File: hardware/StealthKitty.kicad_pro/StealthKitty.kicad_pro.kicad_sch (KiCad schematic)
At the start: 0 parts

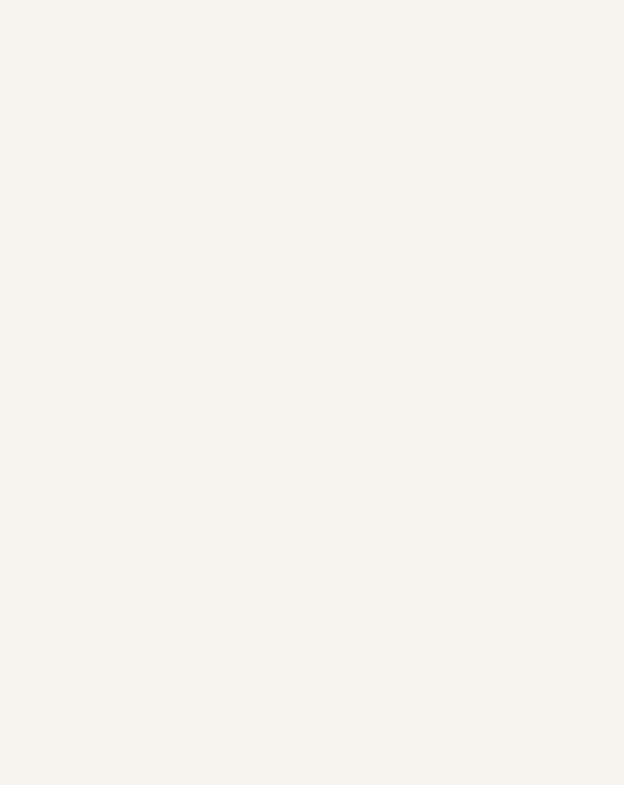
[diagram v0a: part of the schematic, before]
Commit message: réassignation pins stm32, ajout des modifs de la partie power, ajout des modfis de la revue de projet 02/10/24, modifs du 3/10/24 voir readme
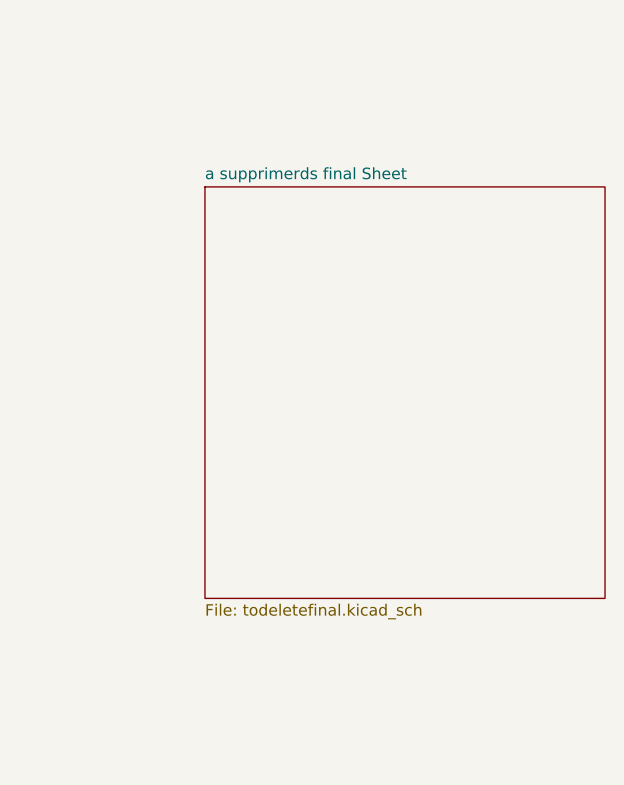
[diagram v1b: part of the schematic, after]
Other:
- added sheet a supprimerds final Sheet (todeletefinal.kicad_sch)
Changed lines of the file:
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@@
 	(paper "A4")
+	(sheet
+		(at 233.68 60.96)
+		(size 44.45 45.72)
+		(fields_autoplaced yes)
+		(stroke
+			(width 0.1524)
+			(type solid)
+		)
+		(fill
+			(color 0 0 0 0.0000)
+		)
+		(property "Sheetname" "a supprimerds final Sheet"
+			(at 233.68 60.2484 0)
+			(effects
+				(font
+					(size 1.27 1.27)
+				)
+				(justify left bottom)
+			)
+		)
+		(property "Sheetfile" "todeletefinal.kicad_sch"
+			(at 233.68 107.2646 0)
+			(effects
+				(font
+					(size 1.27 1.27)
+				)
+				(justify left top)
+			)
+		)
+		(instances
+			(project "StealthKitty.kicad_pro"
+				(path "/23d5732b-7ccb-40aa-85a2-3b18421ac23b"
+					(page "6")
+				)
+			)
+		)
+	)
 	(sheet
 		(at 55.88 31.75)
@@
 		)
 		(instances
-			(project "StealthKitty"
+			(project "StealthKitty.kicad_pro"
 				(path "/23d5732b-7ccb-40aa-85a2-3b18421ac23b"
 					(page "3")
@@
 		)
 		(instances
-			(project "StealthKitty"
+			(project "StealthKitty.kicad_pro"
 				(path "/23d5732b-7ccb-40aa-85a2-3b18421ac23b"
 					(page "4")
@@
 		)
 		(instances
-			(project "StealthKitty"
+			(project "StealthKitty.kicad_pro"
 				(path "/23d5732b-7ccb-40aa-85a2-3b18421ac23b"
 					(page "5")
@@
 		)
 		(instances
-			(project "StealthKitty"
+			(project "StealthKitty.kicad_pro"
 				(path "/23d5732b-7ccb-40aa-85a2-3b18421ac23b"
 					(page "3")

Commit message: suppression sous feuille 6,suppression dossier stealthkitty présent dans /hardware
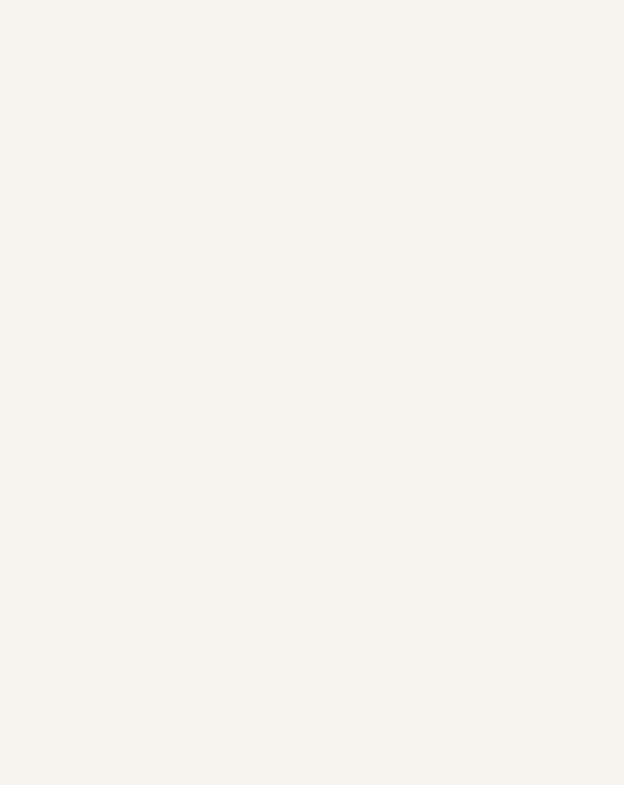
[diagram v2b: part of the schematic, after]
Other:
- removed sheet a supprimerds final Sheet
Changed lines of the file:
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@@
 	(paper "A4")
-	(sheet
-		(at 233.68 60.96)
-		(size 44.45 45.72)
-		(fields_autoplaced yes)
-		(stroke
-			(width 0.1524)
-			(type solid)
-		)
-		(fill
-			(color 0 0 0 0.0000)
-		)
-		(property "Sheetname" "a supprimerds final Sheet"
-			(at 233.68 60.2484 0)
-			(effects
-				(font
-					(size 1.27 1.27)
-				)
-				(justify left bottom)
-			)
-		)
-		(property "Sheetfile" "todeletefinal.kicad_sch"
-			(at 233.68 107.2646 0)
-			(effects
-				(font
-					(size 1.27 1.27)
-				)
-				(justify left top)
-			)
-		)
-		(instances
-			(project "StealthKitty.kicad_pro"
-				(path "/23d5732b-7ccb-40aa-85a2-3b18421ac23b"
-					(page "6")
-				)
-			)
-		)
-	)
 	(sheet
 		(at 55.88 31.75)

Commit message: Modif après revue du prof le 22/10
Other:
- sheet brain Sheet renamed Brain Sheet
- sheet motorisation Sheet renamed Motorisation Sheet
- sheet power Sheet renamed Power Sheet
- sheet sensor Sheet renamed Sensor Sheet
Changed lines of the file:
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@@
 			(color 0 0 0 0.0000)
 		)
-		(property "Sheetname" "motorisation Sheet"
+		(property "Sheetname" "Motorisation Sheet"
 			(at 55.88 29.7684 0)
 			(effects
@@
 			(color 0 0 0 0.0000)
 		)
-		(property "Sheetname" "brain Sheet"
+		(property "Sheetname" "Brain Sheet"
 			(at 137.16 29.7684 0)
 			(effects
@@
 			(color 0 0 0 0.0000)
 		)
-		(property "Sheetname" "power Sheet"
+		(property "Sheetname" "Power Sheet"
 			(at 55.88 90.7284 0)
 			(effects
@@
 			(color 0 0 0 0.0000)
 		)
-		(property "Sheetname" "sensor Sheet"
+		(property "Sheetname" "Sensor Sheet"
 			(at 135.89 90.7284 0)
 			(effects
